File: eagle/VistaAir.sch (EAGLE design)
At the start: 12 parts

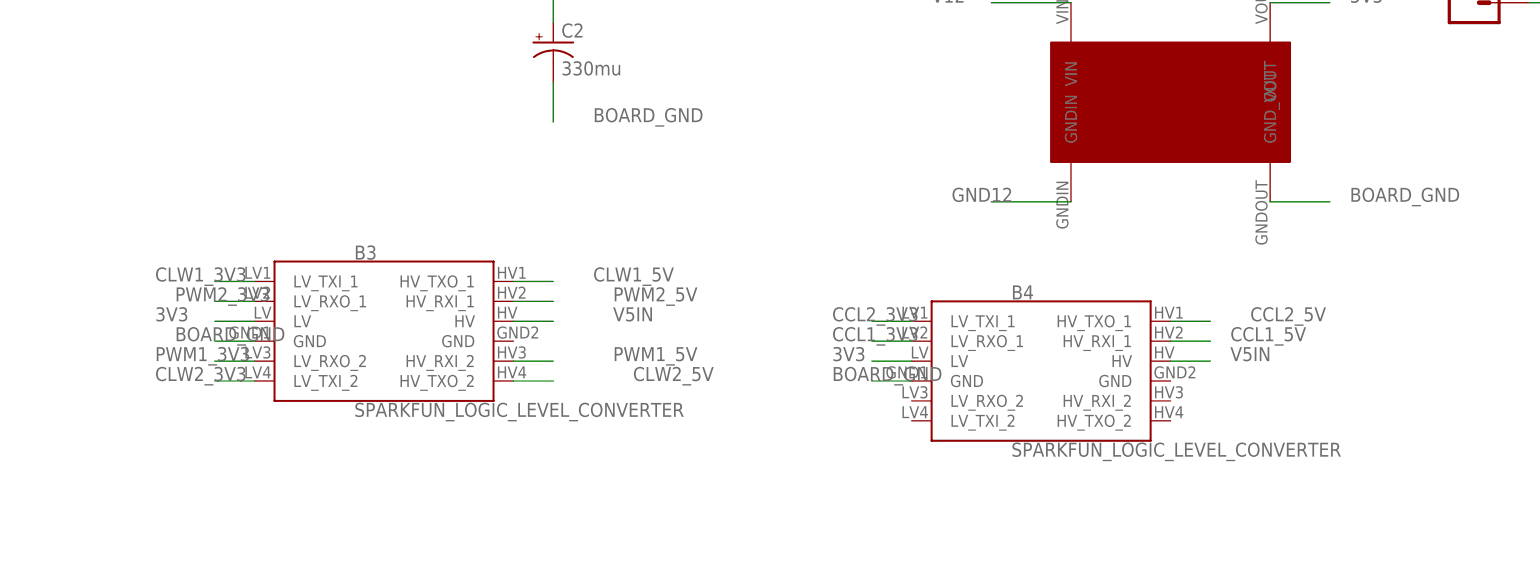
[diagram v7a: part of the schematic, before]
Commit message: board now with working logic converter
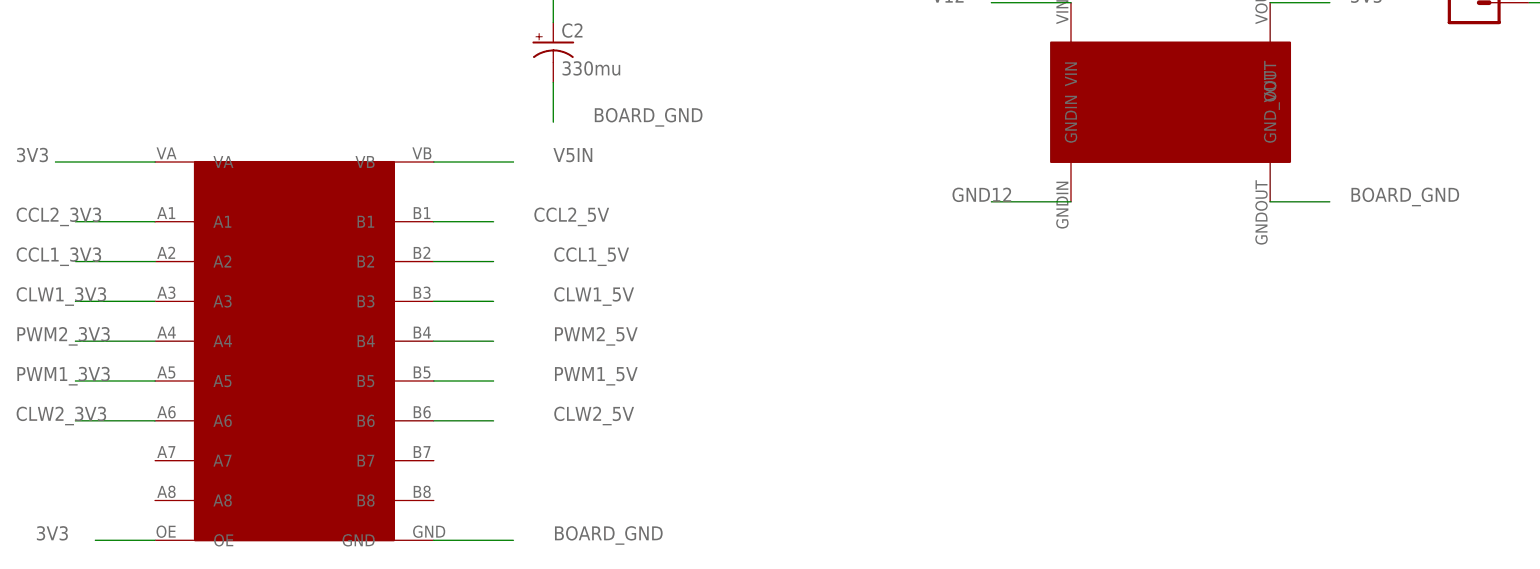
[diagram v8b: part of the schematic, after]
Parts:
- removed B3, B4: SPARKFUN_LOGIC_LEVEL_CONVERTER, SparkFun-Boards:SPARKFUN_LOGIC_LEVEL_CONVERTER
- added U$3: 8_CHANNEL_LOGIC_CONVERTER, kevins_parts:8_CHANNEL_LOGIC_CONVERTER
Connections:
- net 3V3: now also U$3.OE, U$3.VA; no longer B3.LV, B4.LV
- net BOARD_GND: now also U$3.GND; no longer B3.GND, B4.GND
- net CCL1_3V3: now also U$3.A2; no longer B4.LV_RXO_1
- net CCL1_5V: now also U$3.B2; no longer B4.HV_RXI_1
- net CCL2_3V3: now also U$3.A1; no longer B4.LV_TXI_1
- net CCL2_5V: now also U$3.B1; no longer B4.HV_TXO_1
- net CLW1_3V3: now also U$3.A3; no longer B3.LV_TXI_1
- net CLW1_5V: now also U$3.B3; no longer B3.HV_TXO_1
- net CLW2_3V3: now also U$3.A6; no longer B3.LV_TXI_2
- net CLW2_5V: now also U$3.B6; no longer B3.HV_TXO_2
- net PWM1_3V3: now also U$3.A5; no longer B3.LV_RXO_2
- net PWM1_5V: now also U$3.B5; no longer B3.HV_RXI_2
- net PWM2_3V3: now also U$3.A4; no longer B3.LV_RXO_1
- net PWM2_5V: now also U$3.B4; no longer B3.HV_RXI_1
- net V5IN: now also U$3.VB; no longer B3.HV, B4.HV
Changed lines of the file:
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@@
 <part name="U$2" library="kevins_parts" deviceset="LM2596_STEPDOWN_MODULE" device=""/>
 <part name="U$1" library="kevins_parts" deviceset="LDO_REGULATOR_LP2985-N" device=""/>
-<part name="B3" library="SparkFun-Boards" deviceset="SPARKFUN_LOGIC_LEVEL_CONVERTER" device=""/>
-<part name="B4" library="SparkFun-Boards" deviceset="SPARKFUN_LOGIC_LEVEL_CONVERTER" device=""/>
+<part name="U$3" library="kevins_parts" deviceset="8_CHANNEL_LOGIC_CONVERTER" device=""/>
 </parts>
 <sheets>
@@
 <instance part="U$2" gate="G$1" x="99.06" y="-27.94" rot="R270"/>
 <instance part="U$1" gate="G$1" x="83.82" y="30.48"/>
-<instance part="B3" gate="G$1" x="5.08" y="-30.48"/>
-<instance part="B4" gate="G$1" x="88.9" y="-35.56"/>
+<instance part="U$3" gate="G$1" x="5.08" y="-35.56"/>
 </instances>
 <busses>
@@
 </segment>
 <segment>
-<pinref part="B3" gate="G$1" pin="LV_TXI_1"/>
-<wire x1="-12.7" y1="-22.86" x2="-17.78" y2="-22.86" width="0.1524" layer="91"/>
-<label x="-25.4" y="-22.86" size="1.778" layer="95"/>
+<pinref part="U$3" gate="G$1" pin="A3"/>
+<wire x1="-25.4" y1="-25.4" x2="-35.56" y2="-25.4" width="0.1524" layer="91"/>
+<label x="-43.18" y="-25.4" size="1.778" layer="95"/>
 </segment>
 </net>
@@
 </segment>
 <segment>
-<pinref part="B3" gate="G$1" pin="LV_RXO_1"/>
-<wire x1="-12.7" y1="-25.4" x2="-17.78" y2="-25.4" width="0.1524" layer="91"/>
-<label x="-22.86" y="-25.4" size="1.778" layer="95"/>
+<pinref part="U$3" gate="G$1" pin="A4"/>
+<wire x1="-25.4" y1="-30.48" x2="-35.56" y2="-30.48" width="0.1524" layer="91"/>
+<label x="-43.18" y="-30.48" size="1.778" layer="95"/>
 </segment>
 </net>
@@
 </segment>
 <segment>
-<pinref part="B3" gate="G$1" pin="LV_RXO_2"/>
-<wire x1="-12.7" y1="-33.02" x2="-17.78" y2="-33.02" width="0.1524" layer="91"/>
-<label x="-25.4" y="-33.02" size="1.778" layer="95"/>
+<pinref part="U$3" gate="G$1" pin="A5"/>
+<wire x1="-25.4" y1="-35.56" x2="-35.56" y2="-35.56" width="0.1524" layer="91"/>
+<label x="-43.18" y="-35.56" size="1.778" layer="95"/>
 </segment>
 </net>
@@
 </segment>
 <segment>
-<pinref part="B3" gate="G$1" pin="LV_TXI_2"/>
-<wire x1="-12.7" y1="-35.56" x2="-17.78" y2="-35.56" width="0.1524" layer="91"/>
-<label x="-25.4" y="-35.56" size="1.778" layer="95"/>
+<pinref part="U$3" gate="G$1" pin="A6"/>
+<wire x1="-25.4" y1="-40.64" x2="-35.56" y2="-40.64" width="0.1524" layer="91"/>
+<label x="-43.18" y="-40.64" size="1.778" layer="95"/>
 </segment>
 </net>
@@
 </segment>
 <segment>
-<pinref part="B4" gate="G$1" pin="LV_RXO_1"/>
-<wire x1="71.12" y1="-30.48" x2="66.04" y2="-30.48" width="0.1524" layer="91"/>
-<label x="60.96" y="-30.48" size="1.778" layer="95"/>
+<pinref part="U$3" gate="G$1" pin="A2"/>
+<wire x1="-25.4" y1="-20.32" x2="-35.56" y2="-20.32" width="0.1524" layer="91"/>
+<label x="-43.18" y="-20.32" size="1.778" layer="95"/>
 </segment>
 </net>
@@
 </segment>
 <segment>
-<pinref part="B4" gate="G$1" pin="LV_TXI_1"/>
-<wire x1="71.12" y1="-27.94" x2="66.04" y2="-27.94" width="0.1524" layer="91"/>
-<label x="60.96" y="-27.94" size="1.778" layer="95"/>
+<pinref part="U$3" gate="G$1" pin="A1"/>
+<wire x1="-25.4" y1="-15.24" x2="-35.56" y2="-15.24" width="0.1524" layer="91"/>
+<label x="-43.18" y="-15.24" size="1.778" layer="95"/>
 </segment>
 </net>
@@
 </segment>
 <segment>
-<pinref part="B3" gate="G$1" pin="GND"/>
-<wire x1="-12.7" y1="-30.48" x2="-17.78" y2="-30.48" width="0.1524" layer="91"/>
-<label x="-22.86" y="-30.48" size="1.778" layer="95"/>
-</segment>
-<segment>
-<pinref part="B4" gate="G$1" pin="GND"/>
-<wire x1="71.12" y1="-35.56" x2="66.04" y2="-35.56" width="0.1524" layer="91"/>
-<label x="60.96" y="-35.56" size="1.778" layer="95"/>
+<pinref part="U$3" gate="G$1" pin="GND"/>
+<wire x1="10.16" y1="-55.88" x2="20.32" y2="-55.88" width="0.1524" layer="91"/>
+<label x="25.4" y="-55.88" size="1.778" layer="95"/>
 </segment>
 </net>
@@
 </segment>
 <segment>
-<pinref part="B3" gate="G$1" pin="HV"/>
-<wire x1="20.32" y1="-27.94" x2="25.4" y2="-27.94" width="0.1524" layer="91"/>
-<label x="33.02" y="-27.94" size="1.778" layer="95"/>
-</segment>
-<segment>
-<pinref part="B4" gate="G$1" pin="HV"/>
-<wire x1="104.14" y1="-33.02" x2="109.22" y2="-33.02" width="0.1524" layer="91"/>
-<label x="111.76" y="-33.02" size="1.778" layer="95"/>
+<pinref part="U$3" gate="G$1" pin="VB"/>
+<wire x1="10.16" y1="-7.62" x2="20.32" y2="-7.62" width="0.1524" layer="91"/>
+<label x="25.4" y="-7.62" size="1.778" layer="95"/>
 </segment>
 </net>
@@
 </segment>
 <segment>
-<pinref part="B3" gate="G$1" pin="LV"/>
-<wire x1="-12.7" y1="-27.94" x2="-17.78" y2="-27.94" width="0.1524" layer="91"/>
-<label x="-25.4" y="-27.94" size="1.778" layer="95"/>
-</segment>
-<segment>
-<pinref part="B4" gate="G$1" pin="LV"/>
-<wire x1="71.12" y1="-33.02" x2="66.04" y2="-33.02" width="0.1524" layer="91"/>
-<label x="60.96" y="-33.02" size="1.778" layer="95"/>
+<pinref part="U$3" gate="G$1" pin="VA"/>
+<wire x1="-25.4" y1="-7.62" x2="-38.1" y2="-7.62" width="0.1524" layer="91"/>
+<label x="-43.18" y="-7.62" size="1.778" layer="95"/>
+</segment>
+<segment>
+<pinref part="U$3" gate="G$1" pin="OE"/>
+<wire x1="-25.4" y1="-55.88" x2="-33.02" y2="-55.88" width="0.1524" layer="91"/>
+<label x="-40.64" y="-55.88" size="1.778" layer="95"/>
 </segment>
 </net>
@@
 </segment>
 <segment>
-<pinref part="B3" gate="G$1" pin="HV_TXO_2"/>
-<wire x1="20.32" y1="-35.56" x2="25.4" y2="-35.56" width="0.1524" layer="91"/>
-<label x="35.56" y="-35.56" size="1.778" layer="95"/>
+<pinref part="U$3" gate="G$1" pin="B6"/>
+<wire x1="10.16" y1="-40.64" x2="17.78" y2="-40.64" width="0.1524" layer="91"/>
+<label x="25.4" y="-40.64" size="1.778" layer="95"/>
 </segment>
 </net>
@@
 </segment>
 <segment>
-<pinref part="B3" gate="G$1" pin="HV_RXI_2"/>
-<wire x1="20.32" y1="-33.02" x2="25.4" y2="-33.02" width="0.1524" layer="91"/>
-<label x="33.02" y="-33.02" size="1.778" layer="95"/>
+<pinref part="U$3" gate="G$1" pin="B5"/>
+<wire x1="10.16" y1="-35.56" x2="17.78" y2="-35.56" width="0.1524" layer="91"/>
+<label x="25.4" y="-35.56" size="1.778" layer="95"/>
 </segment>
 </net>
@@
 </segment>
 <segment>
-<pinref part="B3" gate="G$1" pin="HV_RXI_1"/>
-<wire x1="20.32" y1="-25.4" x2="25.4" y2="-25.4" width="0.1524" layer="91"/>
-<label x="33.02" y="-25.4" size="1.778" layer="95"/>
+<pinref part="U$3" gate="G$1" pin="B4"/>
+<wire x1="10.16" y1="-30.48" x2="17.78" y2="-30.48" width="0.1524" layer="91"/>
+<label x="25.4" y="-30.48" size="1.778" layer="95"/>
 </segment>
 </net>
@@
 </segment>
 <segment>
-<pinref part="B3" gate="G$1" pin="HV_TXO_1"/>
-<wire x1="20.32" y1="-22.86" x2="25.4" y2="-22.86" width="0.1524" layer="91"/>
-<label x="30.48" y="-22.86" size="1.778" layer="95"/>
+<pinref part="U$3" gate="G$1" pin="B3"/>
+<wire x1="10.16" y1="-25.4" x2="17.78" y2="-25.4" width="0.1524" layer="91"/>
+<label x="25.4" y="-25.4" size="1.778" layer="95"/>
 </segment>
 </net>
@@
 </segment>
 <segment>
-<pinref part="B4" gate="G$1" pin="HV_RXI_1"/>
-<wire x1="104.14" y1="-30.48" x2="109.22" y2="-30.48" width="0.1524" layer="91"/>
-<label x="111.76" y="-30.48" size="1.778" layer="95"/>
+<pinref part="U$3" gate="G$1" pin="B2"/>
+<wire x1="10.16" y1="-20.32" x2="17.78" y2="-20.32" width="0.1524" layer="91"/>
+<label x="25.4" y="-20.32" size="1.778" layer="95"/>
 </segment>
 </net>
@@
 </segment>
 <segment>
-<pinref part="B4" gate="G$1" pin="HV_TXO_1"/>
-<wire x1="104.14" y1="-27.94" x2="109.22" y2="-27.94" width="0.1524" layer="91"/>
-<label x="114.3" y="-27.94" size="1.778" layer="95"/>
-</segment>
-</net>
+<pinref part="U$3" gate="G$1" pin="B1"/>
+<wire x1="10.16" y1="-15.24" x2="17.78" y2="-15.24" width="0.1524" layer="91"/>
+<label x="22.86" y="-15.24" size="1.778" layer="95"/>
+</segment>
+</net>
